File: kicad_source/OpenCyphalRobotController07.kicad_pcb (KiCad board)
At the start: 2 copper layers, 140 x 70 mm, 166 parts, among them J1 SM04B-SRSS-TB, J10 x, J11 PowerPole, J12 Conn_01x02, J13 Conn_01x02, J14 Conn_01x02, J2 RASPBERRYPI_PICO, J3 SM04B-SRSS-TB, J4 S3B-PH-SM4-TB, J5 BM04B-GHS-TBT, J6 BM04B-GHS-TBT, J7 x, J8 x, J9 x, Q1 2N7002, Q2 IPD90P03P4L- 04, SW1 PTS636 SM43 SMTR LFS, U1 24LC64-I/SN, U10 ADS1015IDGS, U11 OPA2374AIDCN, U12 INA226, U13 IFX91041EFJ, U14 ITS4200S-ME-P, U15 ITS4200S-ME-P, U16 BNO085, U2 MCP2515-I/SO, U3 SN65HVD232, U4 74xx08, U5 IFX007T, U6 IFX007T, U7 IFX007T, U8 IFX007T, U9 OPA2374AIDCN, Y1 RH100-16.000-16-3030-EXT-TR, Y2 DNI

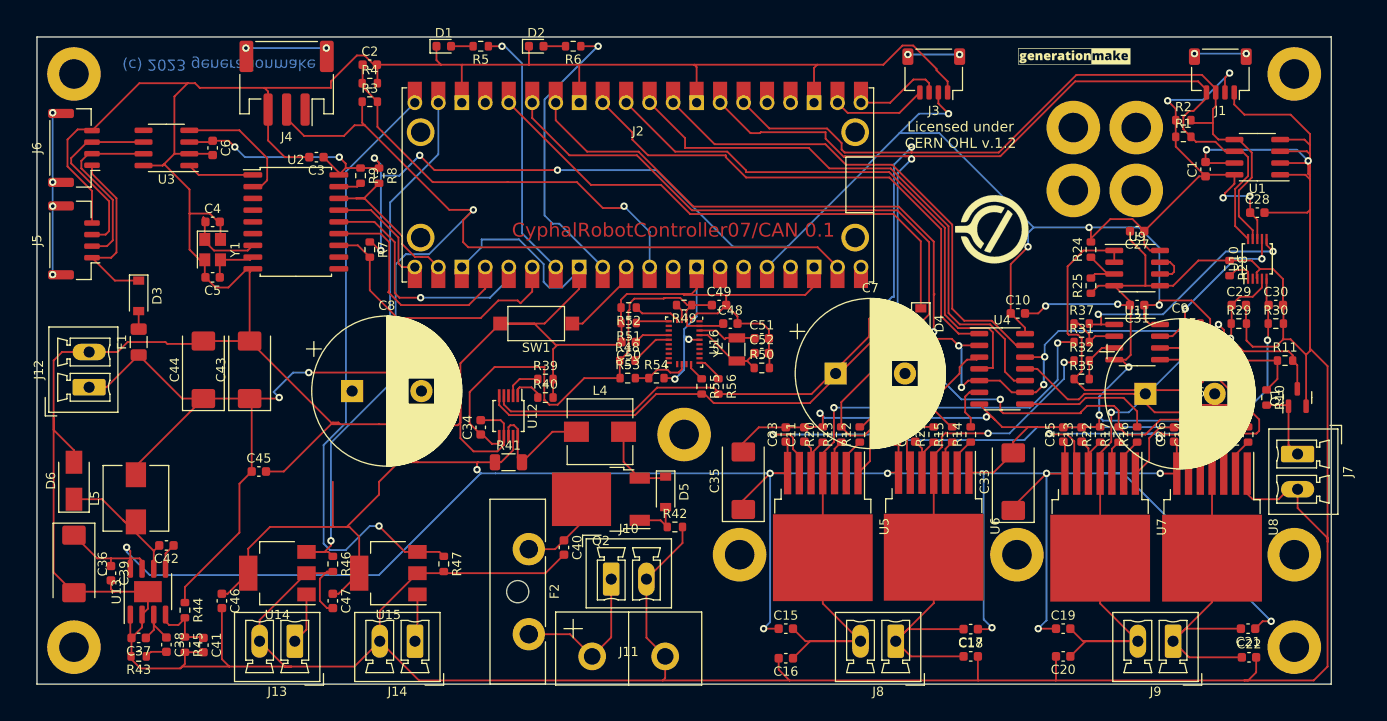
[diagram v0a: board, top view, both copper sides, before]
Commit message: reworked shape of PCB to fit into T07, added hole for USB connector
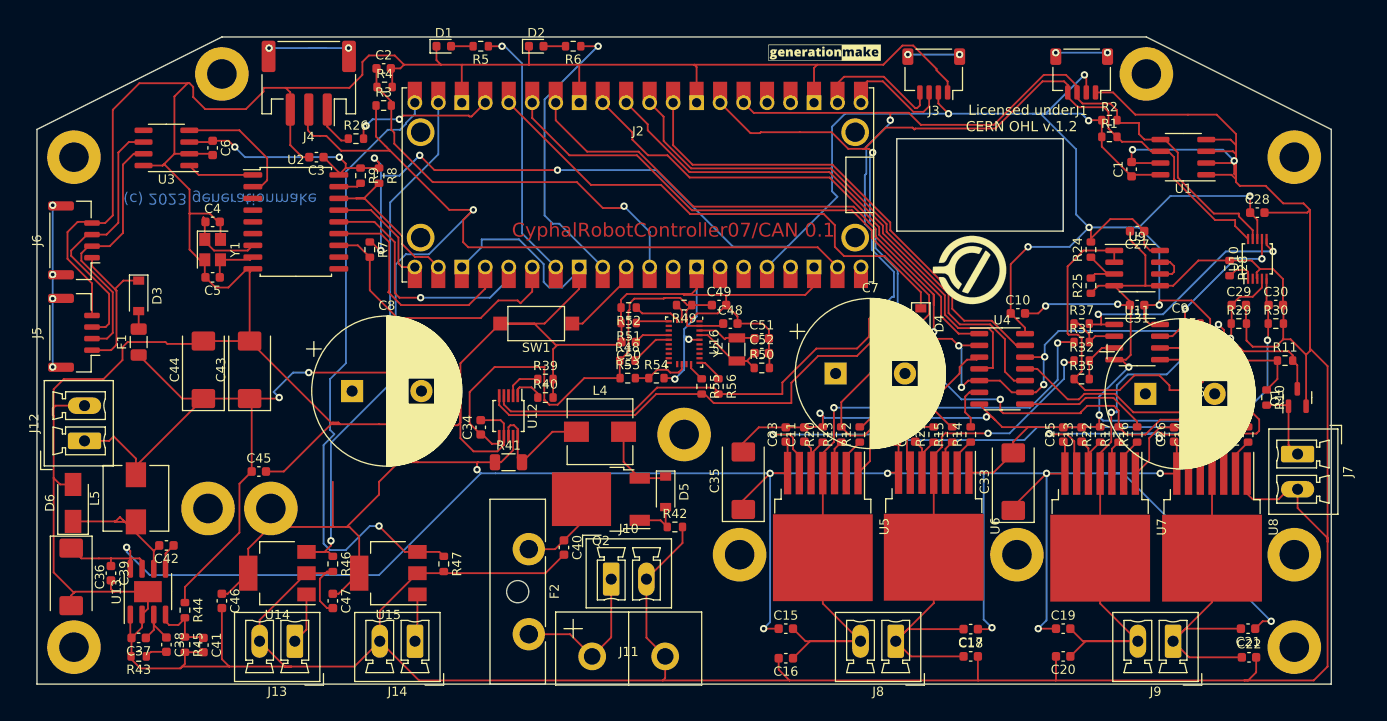
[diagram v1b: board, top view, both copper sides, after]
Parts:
- added R26: 100R, Resistor_SMD:R_0603_1608Metric, F.Cu at (85.5, 67.0)
- moved MECH13 108.5 mm to (69.5, 107.0)
- moved MECH11 108.1 mm to (55.0, 69.0)
- moved MECH14 99.7 mm to (76.3, 107.0)
- moved L2 39.3 mm to (123.5, 60.3)
- moved L1 27.0 mm to (136.2, 60.3)
- moved MECH12 24.2 mm to (187.0, 69.0)
- moved MECH3 16.0 mm to (71.0, 60.0)
- moved MECH4 16.0 mm to (171.0, 60.0)
- moved J1 15.0 mm to (164.0, 60.0)
- moved J5 10.0 mm to (55.0, 88.0)
- moved J6 10.0 mm to (55.0, 78.0)
- moved C1 8.00 mm to (169.4, 70.3)
- moved R1 8.00 mm to (167.0, 66.8)
- moved R2 8.00 mm to (167.0, 65.0)
- moved U1 8.00 mm to (175.0, 69.0)
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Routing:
- net I2C_SCL: track 300.3 -> 144.5 mm, vias 4 -> 2
- net I2C_SDA: track 0.00 -> 143.6 mm, vias 0 -> 2
- net OUT3: track 121.4 -> 59.8 mm
- net /Measurement/VREF: track 0.00 -> 37.0 mm
- net /MotorDriver/PWM4_U: track 0.00 -> 27.9 mm
- net GND: track 969.9 -> 997.6 mm
- net /NEOPIXEL: track 0.00 -> 15.5 mm, vias 0 -> 2
- net +3.3V: track 251.5 -> 263.5 mm, vias 14 -> 13
- net /MCP2515/CANL: track 20.1 -> 28.8 mm
- net /MCP2515/CANH: track 19.6 -> 28.1 mm
- net /NEOPIXEL_R: track 0.00 -> 4.83 mm
- net PWM1: track 57.2 -> 53.3 mm
- net PWM2: track 60.9 -> 57.4 mm
- net /MCP2515/CANVCC: track 19.5 -> 16.6 mm
- net INH12: track 88.2 -> 85.3 mm
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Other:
- outline, holes or cut-outs redrawn

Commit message: added connector for quad encoder
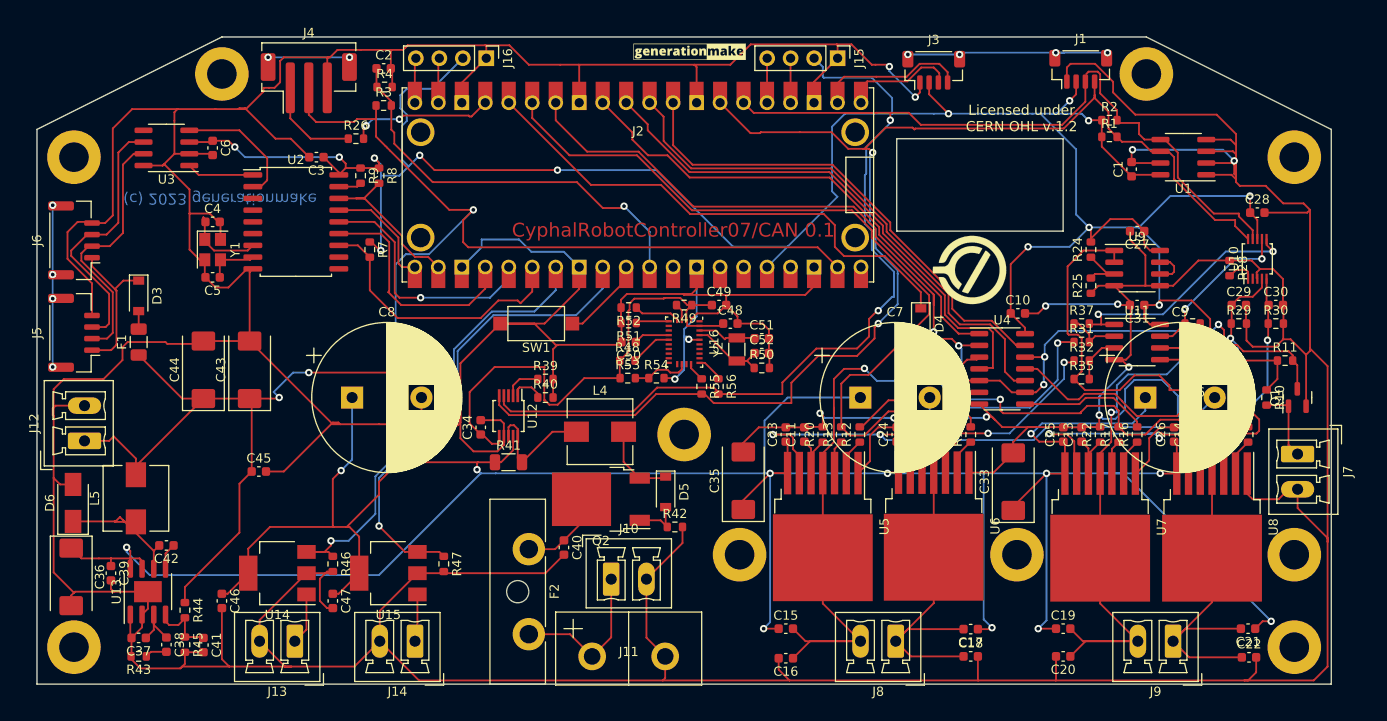
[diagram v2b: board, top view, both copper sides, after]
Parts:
- removed D1: 150060RS75000, LED_SMD:LED_0603_1608Metric
- removed D2: 150060YS75000, LED_SMD:LED_0603_1608Metric
- removed MECH13, MECH14: MHP_3.2_5.0, generationmake:MHP_3.2_5.8
- removed R5, R6: 3k3, Resistor_SMD:R_0603_1608Metric
- added J15: PinHeader_1x04, Connector_PinHeader_2.54mm:PinHeader_1x04_P2.54mm_Vertical, F.Cu at (137.6, 58.3)
- added J16: PinHeader_1x04, Connector_PinHeader_2.54mm:PinHeader_1x04_P2.54mm_Vertical, F.Cu at (99.6, 58.3)
- J1, J3: value SM04B-SRSS-TB -> BM04B-SRSS-TB; footprint Connector_JST:JST_SH_SM04B-SRSS-TB_1x04-1MP_P1.00mm_Horizontal -> Connector_JST:JST_SH_BM04B-SRSS-TB_1x04-1MP_P1.00mm_Vertical
- J4: value S3B-PH-SM4-TB -> B3B-PH-SM4-TB; footprint Connector_JST:JST_PH_S3B-PH-SM4-TB_1x03-1MP_P2.00mm_Horizontal -> Connector_JST:JST_PH_B3B-PH-SM4-TB_1x03-1MP_P2.00mm_Vertical
- moved L1 14.6 mm to (121.6, 60.2)
- moved L2 14.5 mm to (109.0, 60.3)
- moved C7 3.73 mm to (140.1, 95.0)
- moved C8 0.70 mm to (85.1, 95.0)
- moved J1 0.51 mm to (163.9, 59.5), turned to 0 degrees
- moved C9 0.40 mm to (170.9, 95.0)
- moved J3 0.40 mm to (148.0, 59.6), turned to 0 degrees
- turned J4 to 0 degrees
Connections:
- J2 pad 19: OUTPUT0 -> /QUAD2
- J2 pad 20: OUTPUT1 -> /QUAD3
- J2 pad 27: /LED2 -> OUTPUT0
- J2 pad 29: /LED3 -> OUTPUT1
- J2 pad 4: unconnected-(J2-Pad4) -> /QUAD0
- J2 pad 5: unconnected-(J2-Pad5) -> /QUAD1
- J3 pad MP: /MP3 -> /MP2
- J4 pad MP: /MP2 -> /MP3
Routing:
- net +BATT: track 307.3 -> 353.1 mm, vias 10 -> 12
- net /LED3: track 31.2 -> 0.00 mm, vias 1 -> 0
- net /LED2: track 27.9 -> 0.00 mm, vias 1 -> 0
- net +3.3V: track 263.5 -> 289.9 mm
- net GND: track 997.6 -> 1015.8 mm, vias 12 -> 14
- net OUTPUT1: track 68.7 -> 51.6 mm
- net OUTPUT0: track 58.7 -> 50.0 mm
- net /MP2: track 16.0 -> 22.6 mm
- net OUT1: track 74.6 -> 80.7 mm
- net /NEOPIXEL_R: track 4.83 -> 10.5 mm
- net /QUAD3: track 0.00 -> 3.59 mm
- net /QUAD2: track 0.00 -> 3.59 mm
- net /QUAD0: track 0.00 -> 3.54 mm
- net /QUAD1: track 0.00 -> 3.54 mm
- net /MP3: track 5.60 -> 8.80 mm
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
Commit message: finished layout
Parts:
- removed C2: 100nF, Capacitor_SMD:C_0603_1608Metric
- removed R3: 100k, Resistor_SMD:R_0603_1608Metric
- removed R4: 10k, Resistor_SMD:R_0603_1608Metric
- added J17: PinHeader_1x05, Connector_PinHeader_2.54mm:PinHeader_1x05_P2.54mm_Vertical, F.Cu at (139.1, 85.6)
- J2: footprint generationmake:RASPI_PICO_SOLDER_ONLY -> generationmake:RASPI_PICO_SOLDER_Kopie
- moved L1 52.4 mm to (78.0, 89.2)
- moved C46 8.00 mm to (79.0, 117.0)
- moved C47 8.00 mm to (91.0, 117.0)
- moved J13 8.00 mm to (86.9, 121.4)
- moved J14 8.00 mm to (99.9, 121.4)
- moved R46 8.00 mm to (91.0, 113.0)
- moved R47 8.00 mm to (103.0, 113.0)
- moved U14 8.00 mm to (85.0, 114.0)
- moved U15 8.00 mm to (97.0, 114.0)
- moved C44 7.71 mm to (67.2, 99.5), turned to 0 degrees
- moved C43 7.24 mm to (67.2, 94.5), turned to 0 degrees
- moved C32 6.97 mm to (98.5, 101.3)
- moved C40 6.87 mm to (108.8, 104.4), turned to 180 degrees
- moved J11 6.00 mm to (121.0, 123.0)
- moved C45 5.90 mm to (69.1, 103.1)
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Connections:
- J2 pad 31: /+BATT_MEAS -> /ANALOG_INPUT0
- J2 pad 32: /ANALOG_INPUT0 -> /ANALOG_INPUT1
- J2 pad 34: /ANALOG_INPUT1 -> /ANALOG_INPUT2
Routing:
- net /+BATT_MEAS: track 44.5 -> 0.00 mm, vias 1 -> 0
- net +BATT: track 353.1 -> 310.5 mm, vias 12 -> 13
- net +5V: track 174.9 -> 153.5 mm, vias 4 -> 2
- net +3.3V: track 289.9 -> 307.3 mm, vias 13 -> 11
- net /ANALOG_INPUT1: track 0.00 -> 15.5 mm, vias 0 -> 1
- net /ANALOG_INPUT0: track 0.00 -> 14.9 mm, vias 0 -> 1
- net /ANALOG_INPUT2: track 0.00 -> 12.7 mm, vias 0 -> 1
- net +3V3: track 55.2 -> 46.2 mm, vias 0 -> 2
- net /VoltageRegulator/BUO: track 17.0 -> 10.6 mm
- net IS12: track 82.1 -> 86.7 mm
- net /VoltageRegulator/+BATT_Q: track 9.43 -> 13.6 mm
- net OUTPUT0: track 50.0 -> 46.4 mm, vias 1 -> 2
- net /VoltageRegulator/+BATT_I: track 8.62 -> 11.8 mm
- net OUTPUT1: track 51.6 -> 48.5 mm, vias 1 -> 2
- net MCP2515_INT: track 29.1 -> 26.5 mm
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- added copper zone on B.Cu, net GND
- added copper zone on F.Cu, net GND
- added copper zone on B.Cu, net OUT1
- added copper zone on F.Cu, net OUT1
- added copper zone on B.Cu, net OUT2
- added copper zone on F.Cu, net OUT2
- added copper zone on B.Cu, net OUT3
- added copper zone on F.Cu, net OUT3
- added copper zone on B.Cu, net OUT4
- added copper zone on F.Cu, net OUT4
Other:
- outline, holes or cut-outs redrawn
- board text added: "bot"
- board text added: "top"
- board text removed: "Licensed under CERN OHL v.1.2"
